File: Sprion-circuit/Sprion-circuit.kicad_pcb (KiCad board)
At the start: 2 copper layers, 107.5 x 72 mm, 116 parts, among them IC1 R3111N211A, IC2 TAR5SB50, IC5 NJU6080F1, IC6 NJU6080F1, IC7 NJU6080F1, IC8 NJU6080F1, J1 Conn_01x03_Female, J2 Conn_01x04_Female, J3 Conn_02x03_Odd_Even, J4 Conn_02x03_Odd_Even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

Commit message: fix: eschemaの微修正
ハイサイドスイッチをNch→Pchへ修正
bootをプルダウンに
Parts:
- added R1: 10k, Resistor_SMD:R_0603_1608Metric, F.Cu at (96.5, 68.5)
- Q2: value IRFML8244 -> IRML6402
- moved R24 173.7 mm to (174.7, 62.3), turned to 270 degrees
- moved C15 173.0 mm to (173.2, 65.3), turned to 270 degrees
- moved R25 170.4 mm to (174.7, 65.3), turned to 270 degrees
- moved R18 132.4 mm to (178.2, 126.2), turned to 90 degrees
- moved IC5 124.0 mm to (180.9, 125.9)
- moved D8 120.4 mm to (159.0, 102.2), turned to 172 degrees
- moved C5 98.9 mm to (108.5, 90.3)
- moved RS2 97.0 mm to (108.6, 81.1)
- moved MD2 96.8 mm to (108.4, 88.3), turned to 180 degrees
- moved D2 95.5 mm to (162.8, 102.8), turned to 172 degrees
- moved U5 90.3 mm to (108.9, 83.2), turned to 180 degrees
- moved D3 89.2 mm to (162.9, 45.1), turned to 8 degrees
- moved RS1 84.5 mm to (108.7, 60.9)
- moved R20 83.8 mm to (204.3, 91.0), turned to 90 degrees
- moved C2 78.3 mm to (108.8, 85.0)
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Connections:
- J2 pad 1: /Controller/RESET -> /Controller/SWDCLK
- J2 pad 2: /Controller/SWDIO -> GND
- J2 pad 3: /Controller/SWDCLK -> /Controller/SWDIO
- J2 pad 4: GND -> /Controller/RESET
- Q2 pad 2: +BATT -> Net-(C8-Pad1)
- Q2 pad 3: Net-(C8-Pad1) -> +BATT
- U3 pad 60: GND -> Net-(R1-Pad1)

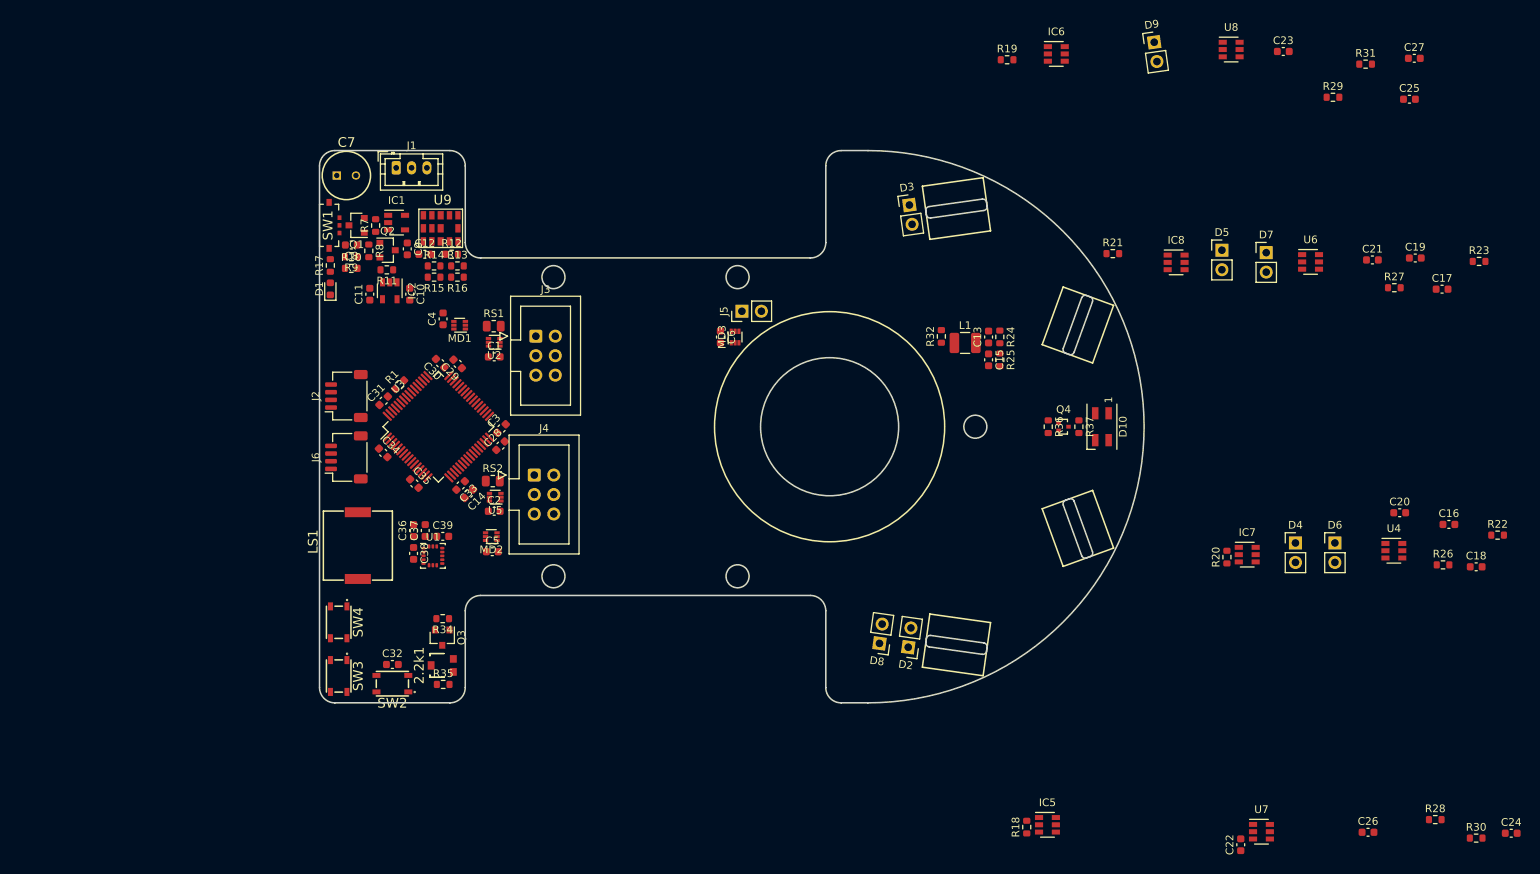
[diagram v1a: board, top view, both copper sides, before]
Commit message: fix add: 配置 回路の修正
nju6080の出力の修正
配置を完了
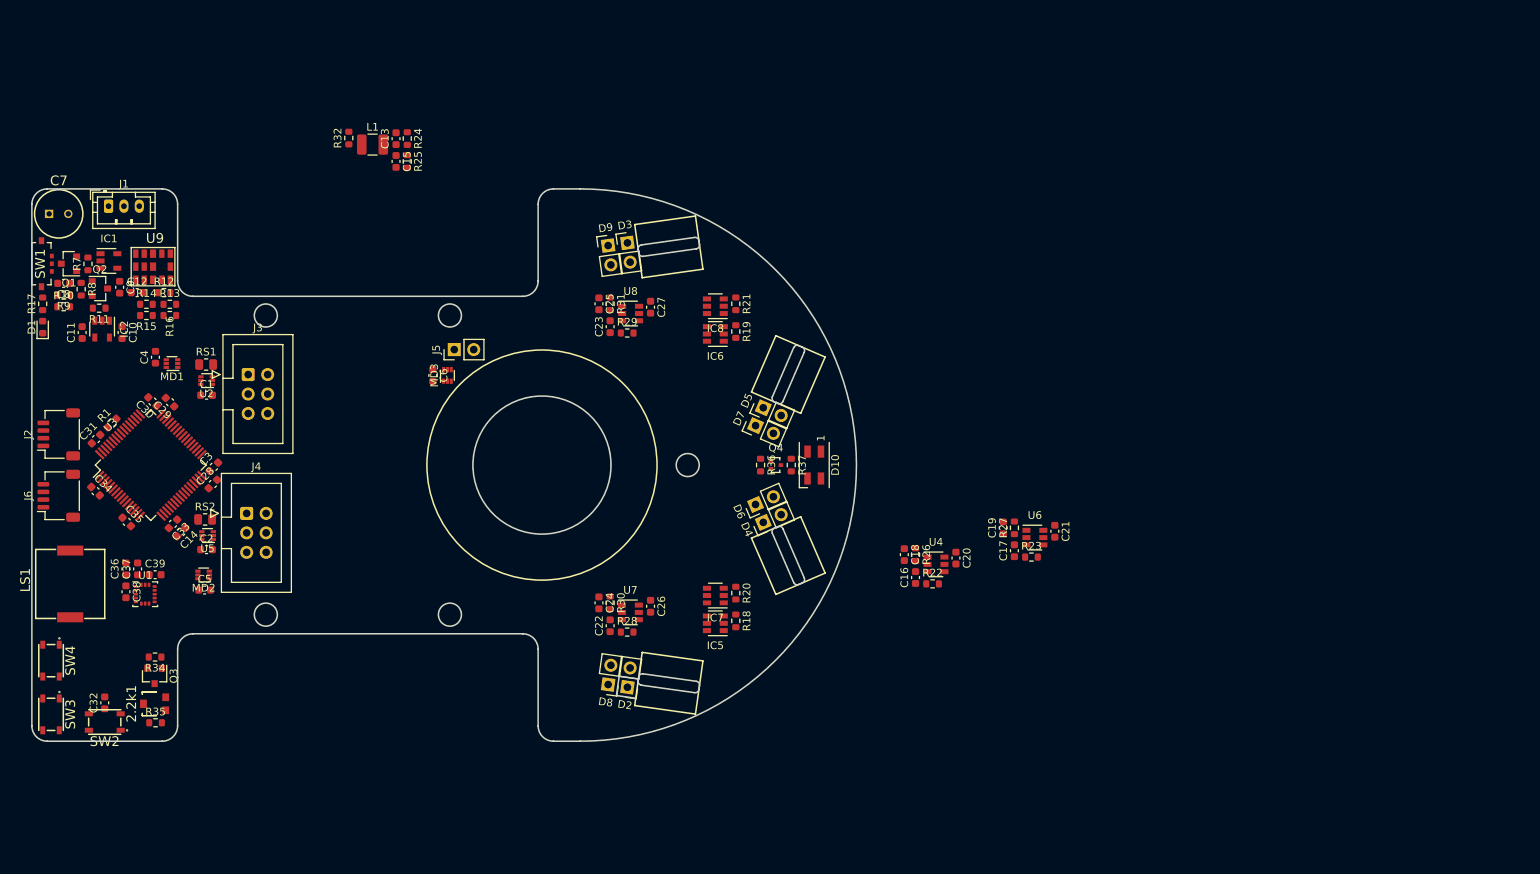
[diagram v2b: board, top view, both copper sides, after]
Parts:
- moved C24 122.7 mm to (122.4, 97.0), turned to 270 degrees
- moved R30 117.0 mm to (123.9, 97.0), turned to 270 degrees
- moved C25 109.0 mm to (122.4, 58.0), turned to 270 degrees
- moved R28 108.1 mm to (126.1, 100.8)
- moved C27 104.7 mm to (129.2, 58.4), turned to 270 degrees
- moved R31 103.3 mm to (123.9, 58.0), turned to 270 degrees
- moved C26 98.1 mm to (129.2, 97.4), turned to 270 degrees
- moved R29 97.0 mm to (126.1, 61.8)
- moved C23 94.8 mm to (123.9, 61.0), turned to 90 degrees
- moved U7 87.1 mm to (126.5, 98.2)
- moved C22 87.0 mm to (123.9, 99.9)
- moved U8 85.5 mm to (126.6, 59.2)
- moved C13 81.5 mm to (96.0, 36.4)
- moved C15 81.5 mm to (96.0, 39.4)
- moved L1 81.5 mm to (92.9, 37.2)
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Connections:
- D2 pad 1: GND -> Net-(D2-Pad1)
- D2 pad 2: Net-(D2-Pad2) -> +3V3
- D3 pad 1: GND -> Net-(D3-Pad1)
- D3 pad 2: Net-(D3-Pad2) -> +3V3
- D4 pad 1: GND -> Net-(D4-Pad1)
- D4 pad 2: Net-(D4-Pad2) -> +3V3
- D5 pad 1: GND -> Net-(D5-Pad1)
- D5 pad 2: Net-(D5-Pad2) -> +3V3
- IC5 pad 4: Net-(D2-Pad2) -> Net-(D2-Pad1)
- IC6 pad 4: Net-(D3-Pad2) -> Net-(D3-Pad1)
- IC7 pad 4: Net-(D4-Pad2) -> Net-(D4-Pad1)
- IC8 pad 4: Net-(D5-Pad2) -> Net-(D5-Pad1)
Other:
- outline, holes or cut-outs redrawn

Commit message: feat: 配置の変更
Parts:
- moved L1 63.1 mm to (113.2, 96.9)
- moved R24 63.1 mm to (117.8, 96.1)
- moved R25 63.1 mm to (117.8, 99.1)
- moved C15 63.1 mm to (116.3, 99.1)
- moved R32 63.1 mm to (110.1, 96.1)
- moved C13 63.1 mm to (116.3, 96.1)
- moved C19 47.1 mm to (132.0, 68.1)
- moved R23 47.1 mm to (135.7, 71.9)
- moved R27 47.1 mm to (133.5, 68.1)
- moved C17 47.1 mm to (133.5, 71.1)
- moved C21 47.1 mm to (138.7, 68.6)
- moved U6 47.1 mm to (136.1, 69.4)
- moved C16 30.5 mm to (133.5, 89.8)
- moved C18 30.5 mm to (132.0, 86.8)
- moved C20 30.5 mm to (138.7, 87.2)
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
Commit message: add fix feat: でけたー（コミットしてなくてごめん）
ベタ塗、配線、再配置等
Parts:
- removed J2: Conn_01x04_Female, Connector_JST:JST_SH_SM04B-SRSS-TB_1x04-1MP_P1.00mm_Horizontal
- added SWD: Conn_01x04_Female, Connector_JST:JST_SH_SM04B-SRSS-TB_1x04-1MP_P1.00mm_Horizontal, F.Cu at (52.0, 72.0)
- D10: footprint LED_SMD:LED_SK6812MINI_PLCC4_3.5x3.5mm_P1.75mm -> Sprion-circuit:SK6812MINI
- J3, J4: footprint Connector_IDC:IDC-Header_2x03_P2.54mm_Vertical -> Sprion-circuit:1717CXR+IE2-4096
- MD1, MD2, MD3, U2, U5: footprint Package_TO_SOT_SMD:SOT-563 -> Sprion-circuit:SOT-563
- Q2: value IRML6402 -> IRFML8244
- moved C14 19.9 mm to (62.3, 68.6), turned to 135 degrees
- moved MD3 17.6 mm to (117.5, 57.8)
- moved C6 17.6 mm to (115.6, 57.8)
- moved C4 17.3 mm to (78.1, 75.8), turned to 0 degrees
- moved MD1 16.5 mm to (78.2, 77.7)
- moved R13 15.2 mm to (52.8, 64.7)
- moved C29 15.1 mm to (53.7, 78.8), turned to 225 degrees
- moved R1 14.7 mm to (56.9, 88.1), turned to 135 degrees
- moved C3 14.5 mm to (61.3, 69.7), turned to 135 degrees
- moved C30 14.5 mm to (51.9, 78.4), turned to 225 degrees
- moved R14 13.4 mm to (52.8, 66.2), turned to 180 degrees
- moved C28 13.1 mm to (64.5, 70.8), turned to 135 degrees
- moved R12 12.9 mm to (55.8, 64.7)
- moved U9 12.9 mm to (56.6, 59.6)
- moved C38 12.8 mm to (54.6, 106.8)
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- renumbered SW2 to RESET, J6 to UART
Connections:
- C7 pad 2: GND -> Net-(C7-Pad2)
- C8 pad 1: Net-(C8-Pad1) -> +BATT
- C8 pad 2: GND -> Net-(C7-Pad2)
- D10 pad 2: GND -> +5V
- D10 pad 4: +5V -> GND
- IC1 pad 3: GND -> Net-(C7-Pad2)
- J1 pad 1: GND -> Net-(C7-Pad2)
- Q1 pad 3: Net-(C8-Pad1) -> +BATT
- Q2 pad 2: Net-(C8-Pad1) -> Net-(C7-Pad2)
- Q2 pad 3: +BATT -> GND
- Q4 pad 3: Net-(D10-Pad3) -> Net-(D10-Pad1)
- R10 pad 2: GND -> Net-(C7-Pad2)
- R11 pad 1: Net-(IC1-Pad1) -> Net-(C7-Pad2)
- R11 pad 2: Net-(C8-Pad1) -> Net-(IC1-Pad1)
- R37 pad 2: Net-(D10-Pad3) -> Net-(D10-Pad1)
- R8 pad 1: Net-(C8-Pad1) -> +BATT
- SW1 pad 1: GND -> Net-(C7-Pad2)
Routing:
- net GND: track 0.00 -> 447.9 mm, vias 0 -> 82
- net +3V3: track 0.00 -> 355.9 mm, vias 0 -> 2
- net +3.3VA: track 0.00 -> 215.2 mm, vias 0 -> 4
- net +BATT: track 0.00 -> 145.5 mm, vias 0 -> 5
- net /Controller/IRLED_SIDE: track 0.00 -> 137.1 mm, vias 0 -> 3
- net /Controller/IRLED_FRONT: track 0.00 -> 133.4 mm, vias 0 -> 3
- net VREF: track 0.00 -> 131.8 mm, vias 0 -> 6
- net +5V: track 0.00 -> 129.0 mm, vias 0 -> 1
- net /Controller/SENSOR_WALL_FR: track 0.00 -> 111.2 mm, vias 0 -> 2
- net /Controller/FULLCOLOR_LED: track 0.00 -> 99.9 mm, vias 0 -> 4
- net /Controller/SENSOR_WALL_SR: track 0.00 -> 78.2 mm, vias 0 -> 2
- net /Controller/SENSOR_WALL_FL: track 0.00 -> 73.5 mm
- net /Controller/SENSOR_WALL_SL: track 0.00 -> 68.2 mm
- net /Controller/MD_SUC_IN1: track 0.00 -> 65.9 mm, vias 0 -> 2
- net /Controller/MD_SUC_IN2: track 0.00 -> 63.3 mm, vias 0 -> 2
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- added copper zone on B.Cu, net GND
- added copper zone on F.Cu, net GND
- added copper zone on B.Cu, net Net-(C7-Pad2)
- added copper zone on F.Cu, net Net-(C7-Pad2)
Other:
- outline, holes or cut-outs redrawn
- net class Default: clearance 0.2 -> 0.1524; trace_width 0.25 -> 0.2
- net class Power added: clearance 0.1524, trace_width 0.34, via_dia 0.8, via_drill 0.4
- rule trace_clearance: 0.2 -> 0.1524
- board text added: "ON⇔OFF"
